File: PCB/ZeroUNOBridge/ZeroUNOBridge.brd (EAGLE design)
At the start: 30.2 x 64.4 mm, 19 parts, among them J3 RASPBERRYPI-40-PIN-GPIO, U1 ATMEGA328P_PDIP_EZ

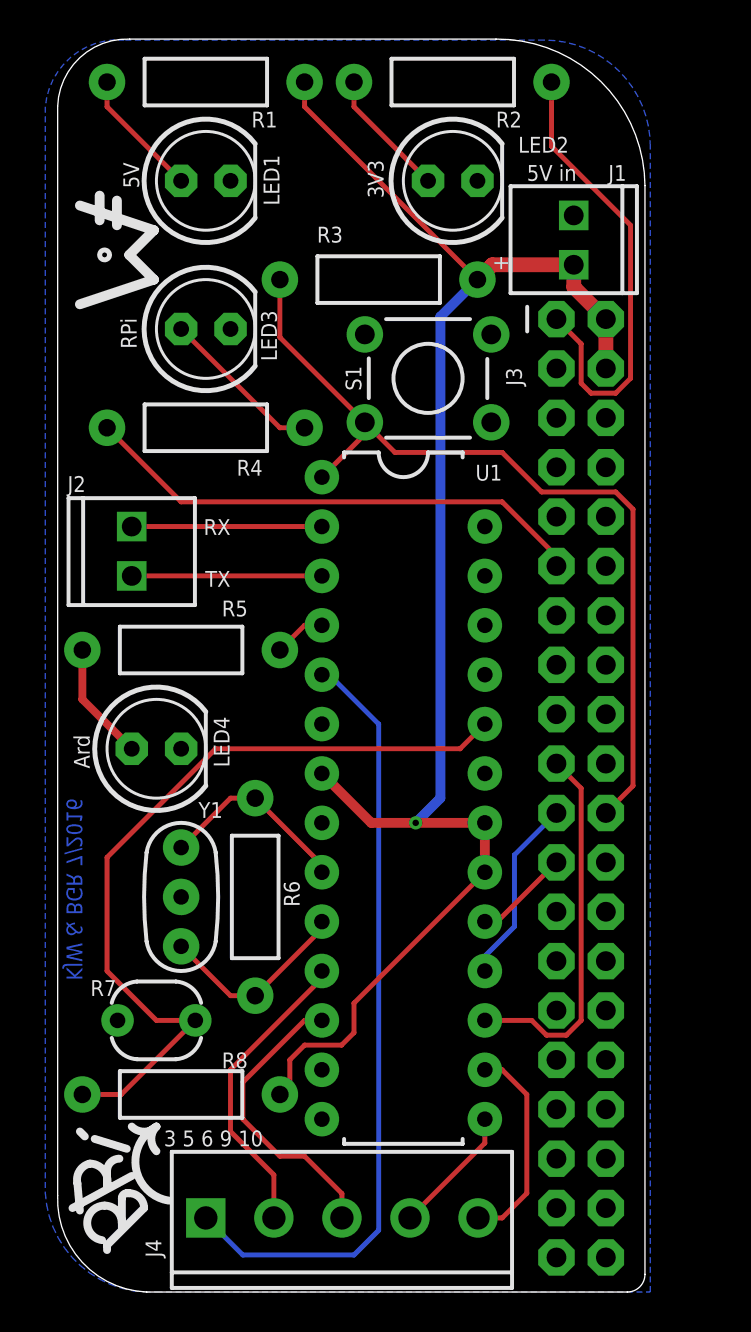
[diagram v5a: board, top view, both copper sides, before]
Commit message: Added level translators so the RPi doesn't blow up
pretty much redid the entire thing - many conversions to SMD
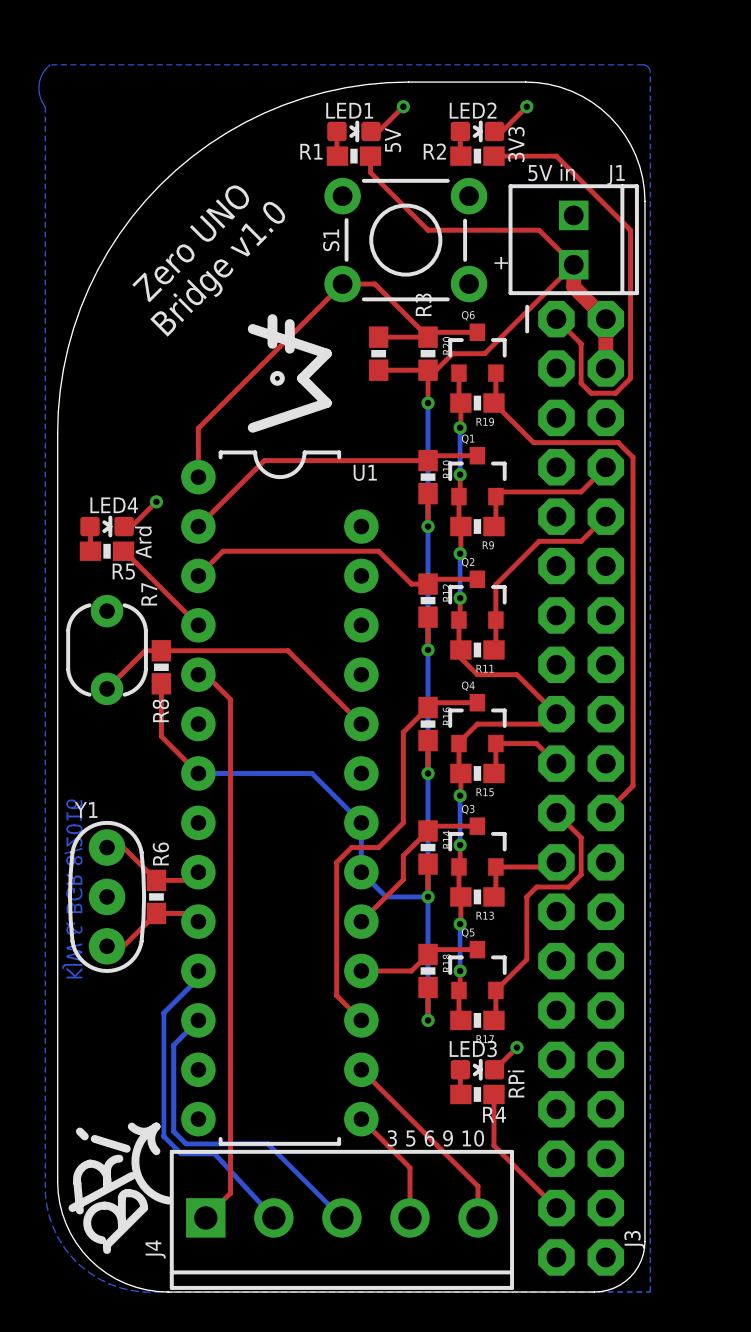
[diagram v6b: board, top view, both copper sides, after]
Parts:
- removed J2: (no value), SparkFun-Connectors:1X02_2.54_SCREWTERM
- added FRAME1: FRAME-LEDGER, SparkFun-Aesthetics:CREATIVE_COMMONS
- added Q1, Q2, Q3, Q4, Q5, Q6: BSS138, SparkFun-DiscreteSemi:SOT23-3
- added R10, R11, R12, R13, R14, R15, R16, R17, R18, R19, R20, R9: 10K, SparkFun-Resistors:0603-RES
- LED1: value (none) -> RED; device adafruit:LED5MM -> SparkFun-LED:LED-0603
- LED2: value (none) -> Yellow; device adafruit:LED5MM -> SparkFun-LED:LED-0603
- LED3: value (none) -> BLUE; device adafruit:LED5MM -> SparkFun-LED:LED-0603
- LED4: value (none) -> GREEN; device adafruit:LED5MM -> SparkFun-LED:LED-0603
- R1, R2, R4, R5: value (none) -> 330; device SparkFun-Resistors:AXIAL-0.4 -> SparkFun-Resistors:0603-RES
- R3, R8: value (none) -> 10K; device SparkFun-Resistors:AXIAL-0.4 -> SparkFun-Resistors:0603-RES
- R6: value (none) -> 1M; device SparkFun-Resistors:AXIAL-0.4 -> SparkFun-Resistors:0603-RES
- moved LED3 40.6 mm to (21.6, 11.4), turned to 270 degrees
- moved R4 37.0 mm to (21.6, 10.2), turned to 0 degrees
- moved R8 22.0 mm to (5.33, 32.1), turned to 270 degrees
- moved R7 19.2 mm to (2.54, 33.0), turned to 270 degrees
- moved LED4 11.7 mm to (2.54, 39.4), turned to 270 degrees
- moved R1 8.52 mm to (15.2, 58.4)
- moved LED1 8.03 mm to (15.2, 59.7), turned to 270 degrees
- moved S1 7.20 mm to (17.9, 54.1)
- moved U1 6.35 mm to (11.4, 25.4)
- moved R5 6.35 mm to (2.54, 38.1)
- moved R6 5.08 mm to (5.08, 20.3)
- moved R2 4.02 mm to (21.6, 58.4)
- moved R3 3.81 mm to (16.5, 48.3), turned to 270 degrees
- moved Y1 3.81 mm to (2.54, 20.3)
- moved LED2 2.84 mm to (21.6, 59.7), turned to 270 degrees
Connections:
- removed net MISO: J3.21, U1.18
- removed net MOSI: J3.19, U1.17
- removed net N$2: J3.11, R4.P$2
- removed net RESET: J3.22, R3.P$1, S1.3, U1.1
- removed net RX: J2.P1, U1.2
- removed net SCLK: J3.23, U1.19
- removed net TX: J2.P2, U1.3
- new net MISO_HV: Q5.3, R18.1, U1.18
- new net MISO_LV: J3.21, Q5.2, R17.1
- new net MOSI_HV: Q4.3, R16.1, U1.17
- new net MOSI_LV: J3.19, Q4.2, R15.1
- new net RESET_HV: Q6.3, R20.1, R3.1, S1.3, U1.1
- new net RESET_LV: J3.22, Q6.2, R19.1
- new net RX_HV: Q1.3, R10.1, U1.2
- new net RX_LV: J3.10, Q2.2, R11.1
- new net SCLK_HV: Q3.3, R14.1, U1.19
- new net SCLK_LV: J3.23, Q3.2, R13.1
- new net TX_HV: Q2.3, R12.1, U1.3
- new net TX_LV: J3.8, Q1.2, R9.1
- net 3.3V: now also J3.1, Q1.1, Q2.1, Q3.1, Q4.1, Q5.1, Q6.1, R11.2, R13.2, R15.2, R17.2, R19.2, R2.1, R9.2
- net 5V: now also R1.1, R10.2, R12.2, R14.2, R16.2, R18.2, R20.2, R3.2, R8.2; no longer R1.P$1, R3.P$2, R8.P$2
- net GND: now also LED1.C, LED2.C, LED3.C, LED4.C; no longer LED1.K, LED2.K, LED3.K, LED4.K
- net N$1: now also J3.37, R4.2; no longer J3.1, R2.P$1
- net N$3: now also R1.2; no longer R1.P$2
- net N$4: now also R2.2; no longer R2.P$2
- net N$5: now also R4.1; no longer R4.P$1
- net N$6: now also R5.1; no longer R5.P$1
- net N$7: now also R5.2; no longer R5.P$2
- net N$9: now also R8.1; no longer R8.P$1
- net XTAL1: now also R6.2; no longer R6.P$2
- net XTAL2: now also R6.1; no longer R6.P$1
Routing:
- net 3.3V: track 0.00 -> 64.2 mm, vias 0 -> 8
- net RESET: track 44.7 -> 0.00 mm
- net RESET_LV: track 0.00 -> 28.8 mm
- net N$2: track 26.4 -> 0.00 mm
- net N$9: track 41.1 -> 15.5 mm
- net RESET_HV: track 0.00 -> 23.7 mm
- net MOSI_HV: track 0.00 -> 22.0 mm
- net MOSI: track 19.3 -> 0.00 mm
- net N$1: track 23.8 -> 7.17 mm
- net RX_HV: track 0.00 -> 15.9 mm
- net TX_HV: track 0.00 -> 15.7 mm
- net MISO_LV: track 0.00 -> 14.0 mm
- net 5V: track 83.3 -> 94.8 mm, vias 1 -> 6
- net PIN3~: track 40.2 -> 29.4 mm
- net RX_LV: track 0.00 -> 10.5 mm
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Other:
- board size 30.2 x 64.4 mm -> 30.2 x 62.2 mm
- board text added: "KJW & BGR 8/2016"
- board text added: "Zero UNO Bridge v1.0"
- board text removed: "J2"
- board text removed: "KJW & BGR 7/2016"
- board text removed: "RX"
- board text removed: "TX"
